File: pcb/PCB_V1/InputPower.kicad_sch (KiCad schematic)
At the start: 22 parts, among them J901 XT60PW-M 24V IN, U902 LMR16020PDDAR

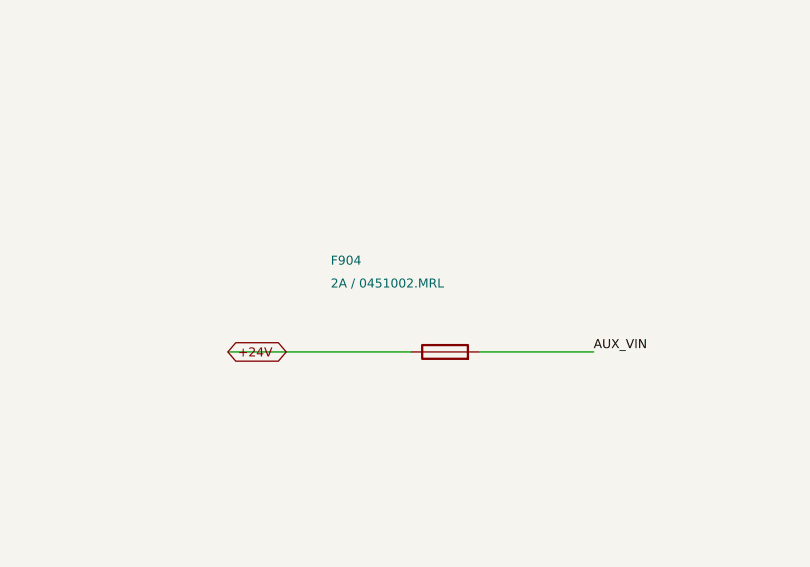
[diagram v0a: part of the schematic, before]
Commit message: pcb: revision 0.19 cost-down in the schematic, same footprints
Schematic and calculations only; PCB_V1.kicad_pcb is untouched on the
user's request. All substitutions keep footprints and nets.

- C716-C719, C726-C728: TDK C3225X7R2A106K250AC (X7R, published DC-bias
  curve 2.35 uF at 49 V) instead of Samsung CL32Y106KCV6PNE.
- C104/C105/C401: Samsung CL21A226MPQNNNE X5R; C521/C710/C715/C725/
  C905/C906: Taiyo Yuden UMK325AB7106KMHP.
- C602 shares CL21A106KAYNNNE with C201 (1.41 uF screen >= 1 uF);
  D601 shares SMBJ26CA with D901 (D_TVS symbol, 42.1 V clamp);
  R501/R511/R521 33R; F904 3 A shared with F721.
- analyze_led_power/analyze_power_path/verify_netlist updated; price and
  JLC snapshots v19; reports, sheet images and checks log v19.
- COST_DOWN.md: USD 37.50 per board (was 39.82), 65 purchase codes,
  rejected candidates and board status.

verify_board.py reports value differences for 17 parts until the board
is synced (footprints and nets already match); all other checks pass.

Co-Authored-By: Claude Opus 5.5 <noreply@anthropic.com>
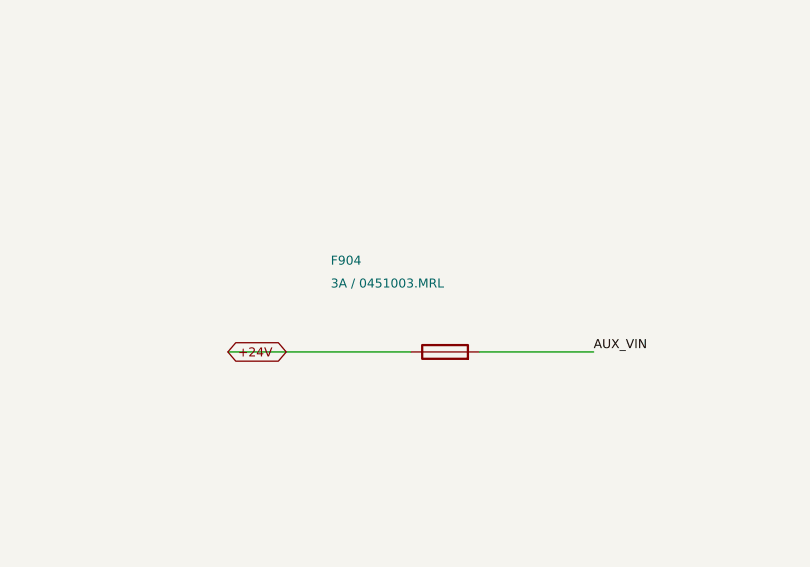
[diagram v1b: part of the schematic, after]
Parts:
- C905, C906: LCSC C77102 -> C386166; MPN GRM32ER71H106KA12L -> UMK325AB7106KMHP; Manufacturer Murata -> Taiyo Yuden
- F904: value 2A / 0451002.MRL -> 3A / 0451003.MRL; LCSC C99547 -> C13982; MPN 0451002.MRL -> 0451003.MRL
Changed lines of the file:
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@@
 			)
 		)
-		(property "Datasheet" ""
+		(property "Datasheet" "https://ds.yuden.co.jp/TYCOMPAS/ut/detail?pn=UMK325AB7106KMHP"
 			(at 33.02 124.46 0)
 			(effects
@@
 			)
 		)
-		(property "Manufacturer" "Murata"
+		(property "Manufacturer" "Taiyo Yuden"
 			(at 33.02 124.46 0)
 			(effects
@@
 			)
 		)
-		(property "MPN" "GRM32ER71H106KA12L"
+		(property "MPN" "UMK325AB7106KMHP"
 			(at 33.02 124.46 0)
 			(effects
@@
 			)
 		)
-		(property "LCSC" "C77102"
+		(property "LCSC" "C386166"
 			(at 33.02 124.46 0)
 			(effects
@@
 			)
 		)
-		(property "Datasheet" ""
+		(property "Datasheet" "https://ds.yuden.co.jp/TYCOMPAS/ut/detail?pn=UMK325AB7106KMHP"
 			(at 50.8 124.46 0)
 			(effects
@@
 			)
 		)
-		(property "Manufacturer" "Murata"
+		(property "Manufacturer" "Taiyo Yuden"
 			(at 50.8 124.46 0)
 			(effects
@@
 			)
 		)
-		(property "MPN" "GRM32ER71H106KA12L"
+		(property "MPN" "UMK325AB7106KMHP"
 			(at 50.8 124.46 0)
 			(effects
@@
 			)
 		)
-		(property "LCSC" "C77102"
+		(property "LCSC" "C386166"
 			(at 50.8 124.46 0)
 			(effects
@@
 			)
 		)
-		(property "Value" "2A / 0451002.MRL"
+		(property "Value" "3A / 0451003.MRL"
 			(at 289.56 76.19999999999999 90)
 			(effects
@@
 			)
 		)
-		(property "MPN" "0451002.MRL"
+		(property "MPN" "0451003.MRL"
 			(at 302.26 83.82 90)
 			(effects
@@
 			)
 		)
-		(property "LCSC" "C99547"
+		(property "LCSC" "C13982"
 			(at 302.26 83.82 90)
 			(effects

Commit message: pcb: revision 0.20 cost-down with new footprints and placement
- RTC: DS3231MZ replaced by NXP PCF8563T/5 with an Epson FC-135 crystal
  (CL 12.5 pF), C304 18 pF C0G on OSCI, BAT54C supply OR (D303) and R307
  1k from the CR2032.
- Boost switches Q711/Q721: AOS AOD66923 (DPAK) on a project footprint
  that keeps the S1/2/3 G4 D5 numbering; diodes D711/D721: Vishay SS5P10
  (TO-277A).
- L101 cjiang FXL0630-100-M and L902 PROD PSPMAA0604-220M-ANP on the
  KiCad FXL0630 land.
- LED switch areas and the RTC cluster re-placed (29 parts moved);
  ERC 0, DRC 0, 340 unrouted links.
- Checks, price/JLC snapshots v20, reports, placement images and docs
  updated: USD 31.62 per board (29.52 for five boards).

Co-Authored-By: Claude Opus 5.5 <noreply@anthropic.com>
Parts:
- L902: value 22u SRP1265A-220M -> 22u PSPMAA0604-220M; footprint GrowBox:L_Bourns_SRP1265A -> Inductor_SMD:L_Changjiang_FXL0630; LCSC C2041465 -> C53190553; MPN SRP1265A-220M -> PSPMAA0604-220M-ANP; Manufacturer Bourns -> PROD Tech
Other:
- note added: "12 V AUX: two fans, UCC27524A, TPS54202 and both AL8853 VIN pins. LMR16020, ~526 kHz (RT 47k), 22 uH PSPMAA0604-220M (Isat 5 A > 3.8 A limit). Vout = 0.75 x (1 + 150k/10k) = 12.00 V; 0.1% divider, static range 11.74..12.26 V. Budget 1.2 A. EN divider 560k/47k retained. C909 100u polymer + C910 22u ceramic; verify startup/load steps and thermal vias. F904 and downstream fuses do not qualify fault 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"
- note added: "External PSU: 24.0 V set point, <=25 V. D901 SMBJ26CA: 26 V standoff, 42.1 V clamp at 14.3 A (25 C). AL8853 VIN pins now use 12 V aux; their power inductors still use 24 V. F902 10 A loads; LED channels fused individually on sheet 07 (F711 6.3 A, F721 3 A); F904 3 A aux. PSU must protect the unfused XT60/TVS input segment."
- note removed: "12 V AUX: two fans, UCC27524A, TPS54202 and both AL8853 VIN pins. LMR16020, ~526 kHz (RT 47k), 22 uH. Vout = 0.75 x (1 + 150k/10k) = 12.00 V; 0.1% divider, static range 11.74..12.26 V. Budget 1.2 A. EN divider 560k/47k retained. C909 100u polymer + C910 22u ceramic; verify startup/load steps and thermal vias. F904 and downstream fuses do not qualify fault clearing; test against the actual PSU and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"
- note removed: "External PSU: 24.0 V set point, <=25 V. D901 SMBJ26CA: 26 V standoff, 42.1 V clamp at 14.3 A (25 C). AL8853 VIN pins now use 12 V aux; their power inductors still use 24 V. F902 10 A loads; LED channels fused individually on sheet 07 (F711 6.3 A, F721 3 A); F904 2 A aux. PSU must protect the unfused XT60/TVS input segment."
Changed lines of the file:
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@@
 		(title "06 - 24 V input, fuses, 12 V auxiliary buck")
 		(date "2026-09-29")
-		(rev "0.18-DRAFT")
+		(rev "0.20-DRAFT")
 		(company "GrowBox controller")
 		(comment 1 "Simplified prototype; unrouted; hardware qualification pending")
@@
 			)
 		)
-		(property "Value" "22u SRP1265A-220M"
+		(property "Value" "22u PSPMAA0604-220M"
 			(at 189.23 116.84 270)
 			(effects
@@
 			)
 		)
-		(property "Footprint" "GrowBox:L_Bourns_SRP1265A"
+		(property "Footprint" "Inductor_SMD:L_Changjiang_FXL0630"
 			(at 195.58 121.92 270)
 			(effects
@@
 			)
 		)
-		(property "Datasheet" ""
+		(property "Datasheet" "https://www.lcsc.com/product-detail/C53190553.html"
 			(at 195.58 121.92 270)
 			(effects
@@
 			)
 		)
-		(property "Manufacturer" "Bourns"
+		(property "Manufacturer" "PROD Tech"
 			(at 195.58 121.92 270)
 			(effects
@@
 			)
 		)
-		(property "MPN" "SRP1265A-220M"
+		(property "MPN" "PSPMAA0604-220M-ANP"
 			(at 195.58 121.92 270)
 			(effects
@@
 			)
 		)
-		(property "LCSC" "C2041465"
+		(property "LCSC" "C53190553"
 			(at 195.58 121.92 270)
 			(effects
@@
 		)
 	)
-	(text "External PSU: 24.0 V set point, <=25 V. D901 SMBJ26CA: 26 V standoff, 42.1 V clamp at 14.3 A (25 C).\nAL8853 VIN pins now use 12 V aux; their power inductors still use 24 V.\nF902 10 A loads; LED channels fused individually on sheet 07 (F711 6.3 A, F721 3 A); F904 2 A aux. PSU must protect the unfused XT60/TVS input segment."
+	(text "External PSU: 24.0 V set point, <=25 V. D901 SMBJ26CA: 26 V standoff, 42.1 V clamp at 14.3 A (25 C).\nAL8853 VIN pins now use 12 V aux; their power inductors still use 24 V.\nF902 10 A loads; LED channels fused individually on sheet 07 (F711 6.3 A, F721 3 A); F904 3 A aux. PSU must protect the unfused XT60/TVS input segment."
 		(exclude_from_sim no)
 		(at 20.32 83.82 0)
@@
 		)
 	)
-	(text "12 V AUX: two fans, UCC27524A, TPS54202 and both AL8853 VIN pins. LMR16020, ~526 kHz (RT 47k), 22 uH.\nVout = 0.75 x (1 + 150k/10k) = 12.00 V; 0.1% divider, static range 11.74..12.26 V. Budget 1.2 A.\nEN divider 560k/47k retained. C909 100u polymer + C910 22u ceramic; verify startup/load steps and thermal vias.\nF904 and downstream fuses do not qualify fault clearing; test against the actual PSU and cables."
+	(text "12 V AUX: two fans, UCC27524A, TPS54202 and both AL8853 VIN pins. LMR16020, ~526 kHz (RT 47k), 22 uH PSPMAA0604-220M (Isat 5 A > 3.8 A limit).\nVout = 0.75 x (1 + 150k/10k) = 12.00 V; 0.1% divider, static range 11.74..12.26 V. Budget 1.2 A.\nEN divider 560k/47k retained. C909 100u polymer + C910 22u ceramic; verify startup/load steps and thermal vias.\nF904 and downstream fuses do not qualify fault clearing; test against the actual PSU and cables."
 		(exclude_from_sim no)
 		(at 20.32 172.72 0)
